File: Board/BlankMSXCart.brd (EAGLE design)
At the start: 100.1 x 58.9 mm, 50 parts, among them CN1 MSXBUS

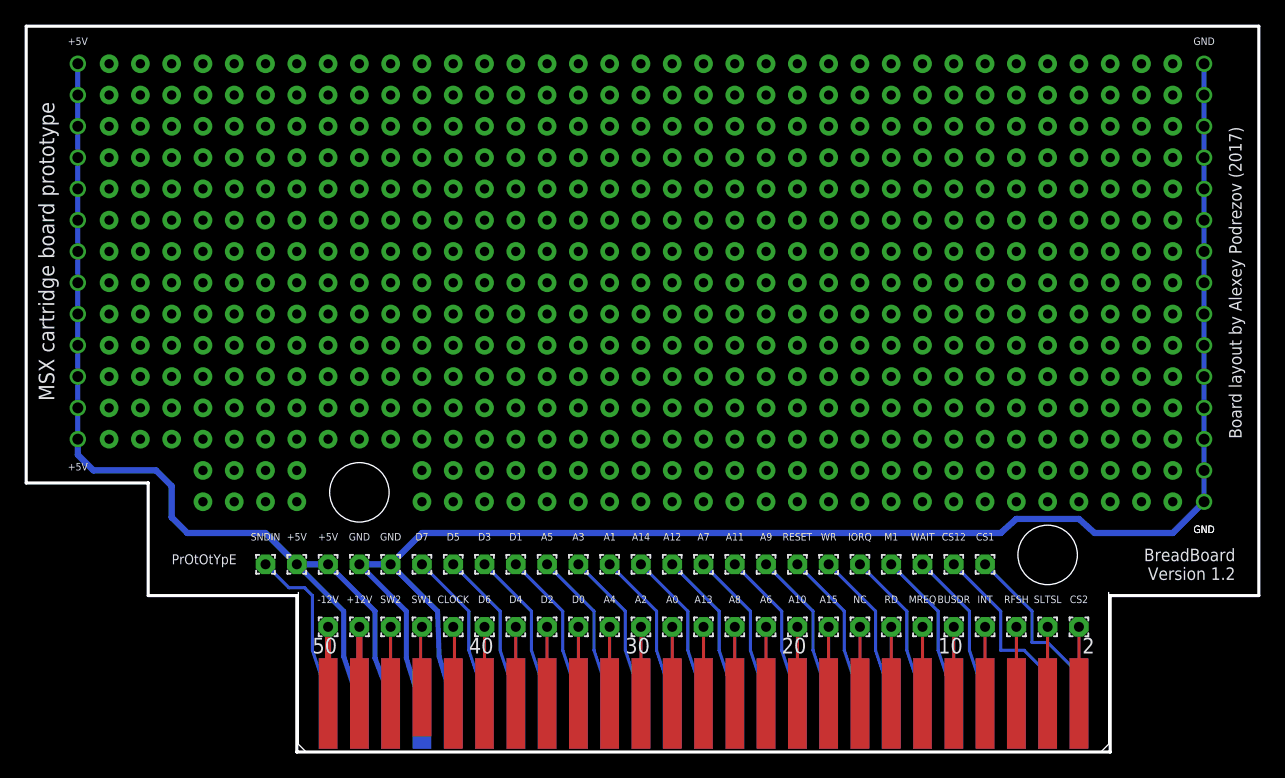
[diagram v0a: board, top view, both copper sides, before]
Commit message: Made the board 1mm narrower for cheaper production
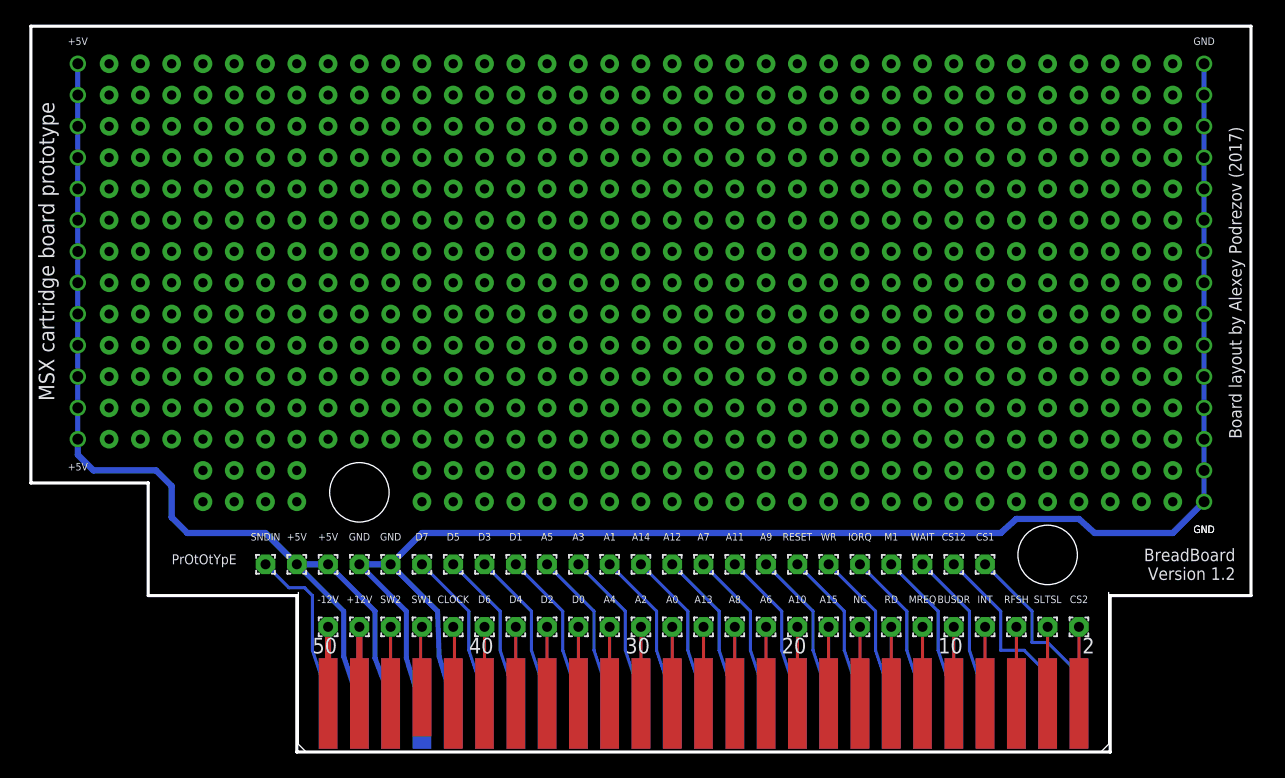
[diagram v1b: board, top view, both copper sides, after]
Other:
- board size 100.1 x 58.9 mm -> 99.1 x 58.9 mm
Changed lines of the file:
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@@
 <board>
 <plain>
-<wire x1="88.9" y1="12.7" x2="100.965" y2="12.7" width="0.254" layer="20"/>
-<wire x1="0.889" y1="58.928" x2="0.889" y2="21.844" width="0.254" layer="20"/>
-<wire x1="0.889" y1="21.844" x2="10.795" y2="21.844" width="0.254" layer="20"/>
+<wire x1="88.9" y1="12.7" x2="100.33" y2="12.7" width="0.254" layer="20"/>
+<wire x1="1.27" y1="58.928" x2="1.27" y2="21.844" width="0.254" layer="20"/>
+<wire x1="1.27" y1="21.844" x2="10.795" y2="21.844" width="0.254" layer="20"/>
 <wire x1="10.795" y1="21.844" x2="10.795" y2="12.7" width="0.254" layer="20"/>
 <wire x1="10.795" y1="12.7" x2="22.86" y2="12.7" width="0.254" layer="20"/>
@@
 <text x="99.06" y="38.1" size="1.016" layer="25" font="vector" rot="R90" align="center">Board layout by Alexey Podrezov (2017)</text>
 <text x="99.06" y="38.1" size="1.016" layer="26" font="vector" rot="MR270" align="center">Board layout by Alexey Podrezov (2017)</text>
-<wire x1="100.965" y1="12.7" x2="100.965" y2="58.928" width="0.254" layer="20"/>
-<wire x1="0.889" y1="58.928" x2="100.965" y2="58.928" width="0.254" layer="20"/>
+<wire x1="100.33" y1="12.7" x2="100.33" y2="58.928" width="0.254" layer="20"/>
+<wire x1="1.27" y1="58.928" x2="100.33" y2="58.928" width="0.254" layer="20"/>
 <text x="27.94" y="17.78" size="0.6096" layer="25" font="vector" align="top-center">GND</text>
 <text x="27.94" y="17.78" size="0.6096" layer="26" font="vector" rot="MR0" align="top-center">GND</text>

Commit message: Updated 10.10.2020
Larger via holes + wider power and ground rails
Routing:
- net GND: track 133.4 -> 205.0 mm
- net +5V: track 83.6 -> 110.4 mm
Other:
- board text added: "BreadBoard Version 1.3"
- board text removed: "BreadBoard Version 1.2"
